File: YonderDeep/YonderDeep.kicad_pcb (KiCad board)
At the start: 2 copper layers, 65 x 56 mm, 5 parts, among them J1 GPIO

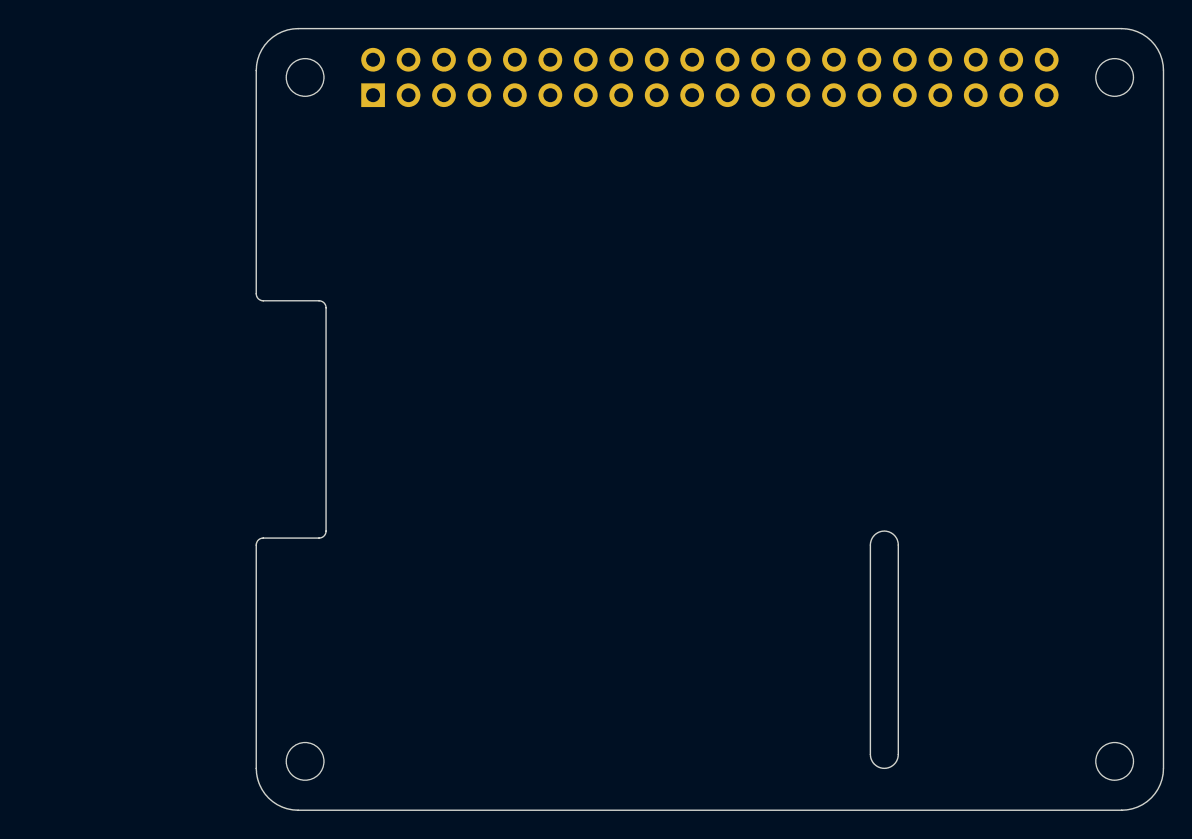
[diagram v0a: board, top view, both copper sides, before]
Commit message: Working on PCB placement
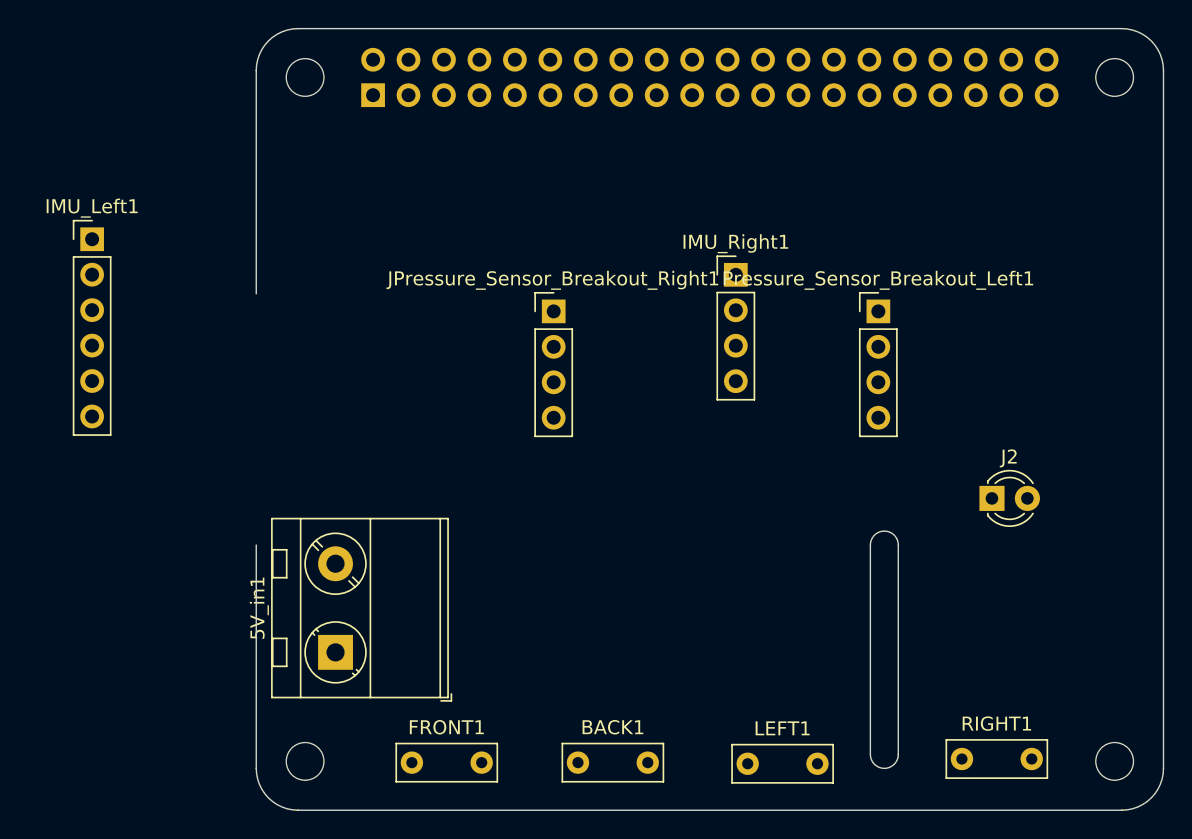
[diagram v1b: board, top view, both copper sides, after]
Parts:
- added 5V_in1: Conn_01x02_Female, TerminalBlock_MetzConnect:TerminalBlock_MetzConnect_Type701_RT11L02HGLU_1x02_P6.35mm_Horizontal, F.Cu at (105.7, 88.7)
- added BACK1: Conn_01x02_Female, Capacitor_THT:C_Rect_L7.0mm_W2.5mm_P5.00mm, F.Cu at (123.0, 96.6)
- added FRONT1: Conn_01x02_Female, Capacitor_THT:C_Rect_L7.0mm_W2.5mm_P5.00mm, F.Cu at (111.2, 96.6)
- added IMU_Left1: Conn_01x06_Female, Connector_PinHeader_2.54mm:PinHeader_1x06_P2.54mm_Vertical, F.Cu at (88.2, 59.1)
- added IMU_Right1: Conn_01x04_Female, Connector_PinHeader_2.54mm:PinHeader_1x04_P2.54mm_Vertical, F.Cu at (134.4, 61.6)
- added J2: Conn_01x02_Female, LED_THT:LED_D3.0mm, F.Cu at (152.7, 77.7)
- added JPressure_Sensor_Breakout_Right1: Conn_01x04_Female, Connector_PinHeader_2.54mm:PinHeader_1x04_P2.54mm_Vertical, F.Cu at (121.3, 64.3)
- added LEFT1: Conn_01x02_Female, Capacitor_THT:C_Rect_L7.0mm_W2.5mm_P5.00mm, F.Cu at (135.2, 96.7)
- added Pressure_Sensor_Breakout_Left1: Conn_01x04_Female, Connector_PinHeader_2.54mm:PinHeader_1x04_P2.54mm_Vertical, F.Cu at (144.6, 64.3)
- added RIGHT1: Conn_01x02_Female, Capacitor_THT:C_Rect_L7.0mm_W2.5mm_P5.00mm, F.Cu at (150.6, 96.3)
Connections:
- net +3V3 renamed 3.3V
- net +5V renamed 5V
- J1 pad 11: /GPIO[17] -> IMU_RST
- J1 pad 12: /GPIO[18]/PCM.CLK -> Back_Motor
- J1 pad 13: /GPIO[27] -> unconnected-(J1-Pad13)
- J1 pad 18: /GPIO[24] -> Front_Motor
- J1 pad 23: /GPIO[11]/SPI0.SCLK -> Right_Motor
- J1 pad 3: /GPIO[2]/SDA1 -> SDA1
- J1 pad 32: /GPIO[12]/PWM0 -> LED_GPIO12
- J1 pad 5: /GPIO[3]/SCL1 -> SCL1
- J1 pad 7: /GPIO[4]/GPCLK0 -> GND
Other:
- outline, holes or cut-outs redrawn
- board text removed: "DISPLAY (OPTIONAL)"
